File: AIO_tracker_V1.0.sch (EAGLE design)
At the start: 60 parts, among them IC1 TPS61201, IC2 TPS61201, J1 AVR_SPI_PRG_6PTH, Q1 MOSFET-PCHANNELSMD, U1 ATMEGA328P-AU, U2 USD-SOCKETNEW

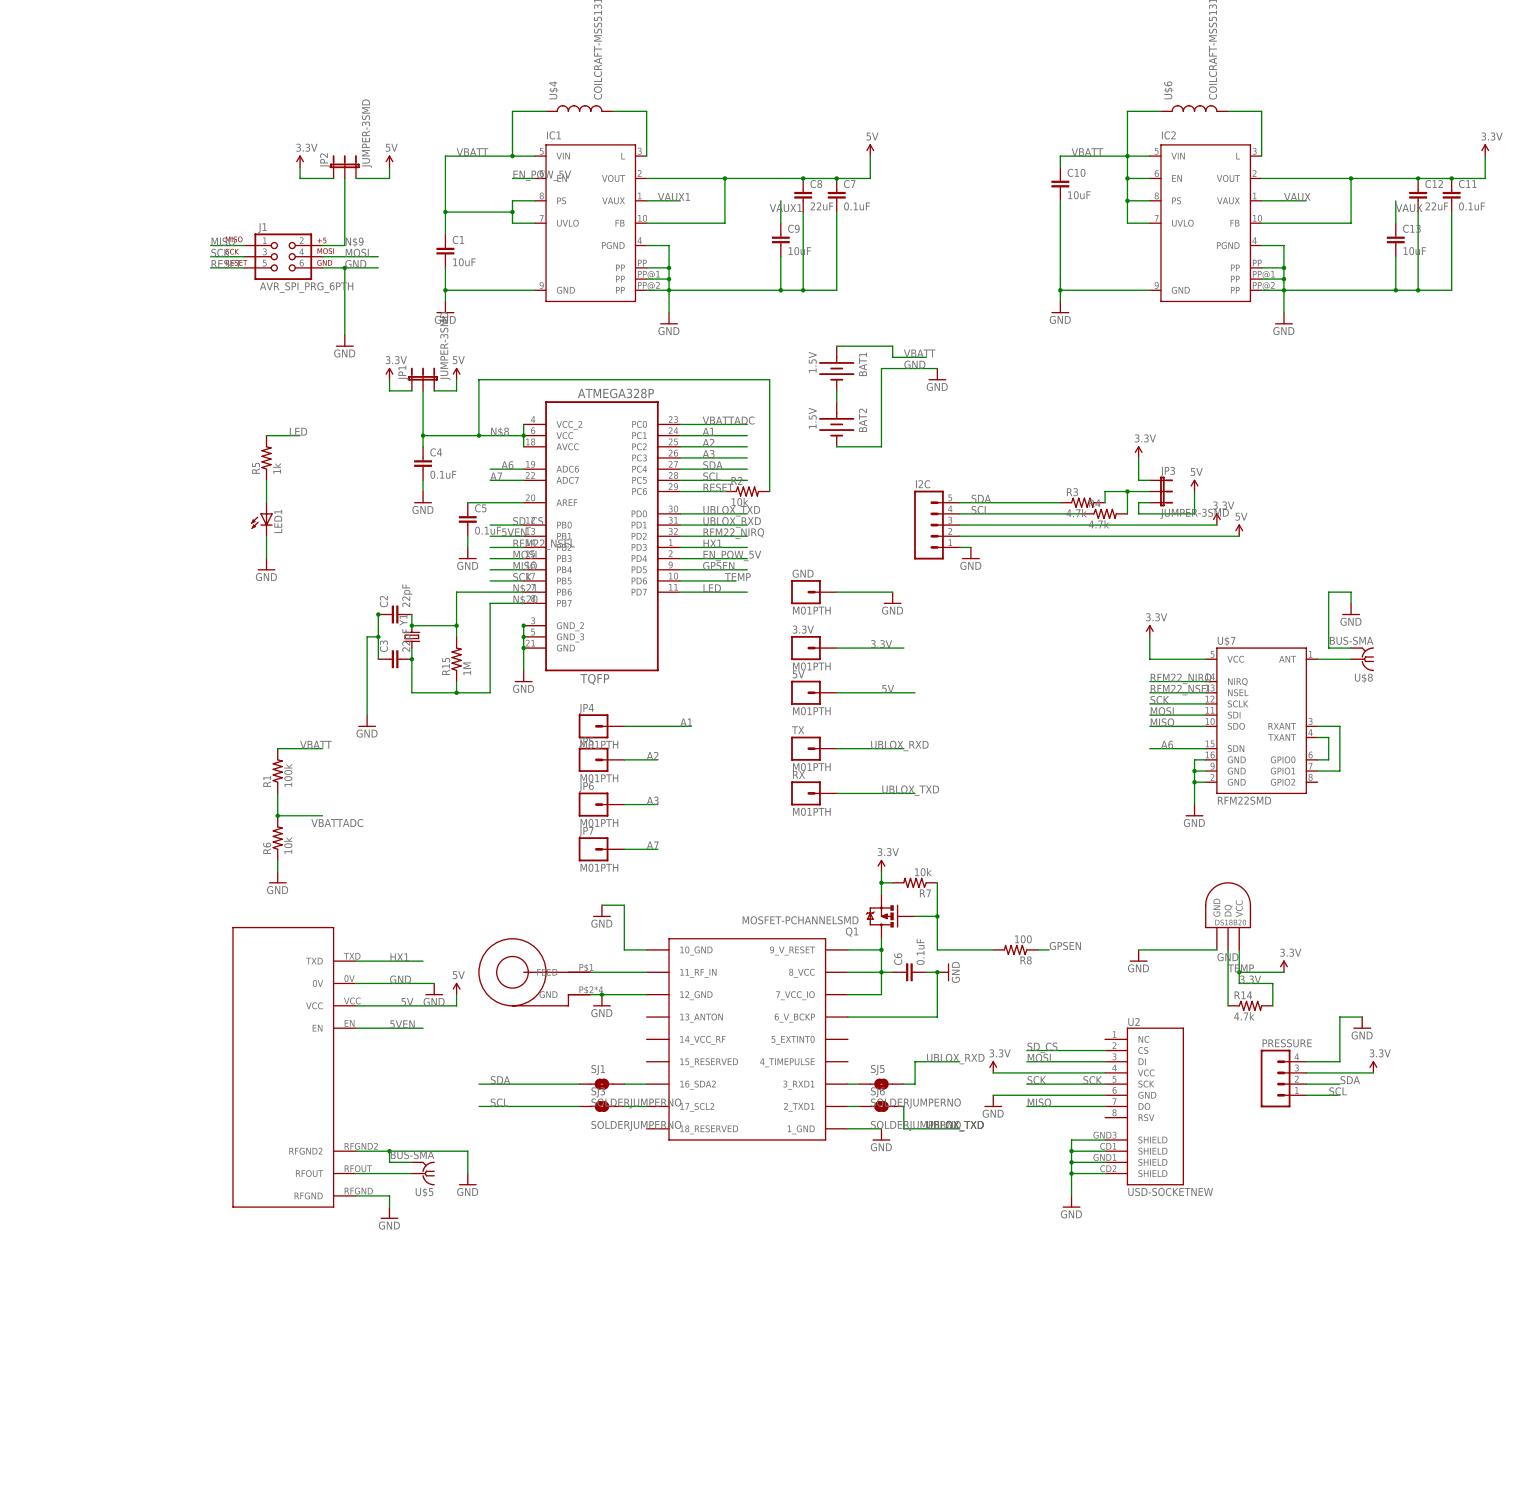
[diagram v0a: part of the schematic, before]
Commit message: Added NTX2 Support option
Added NTX2 Support option and finished routing
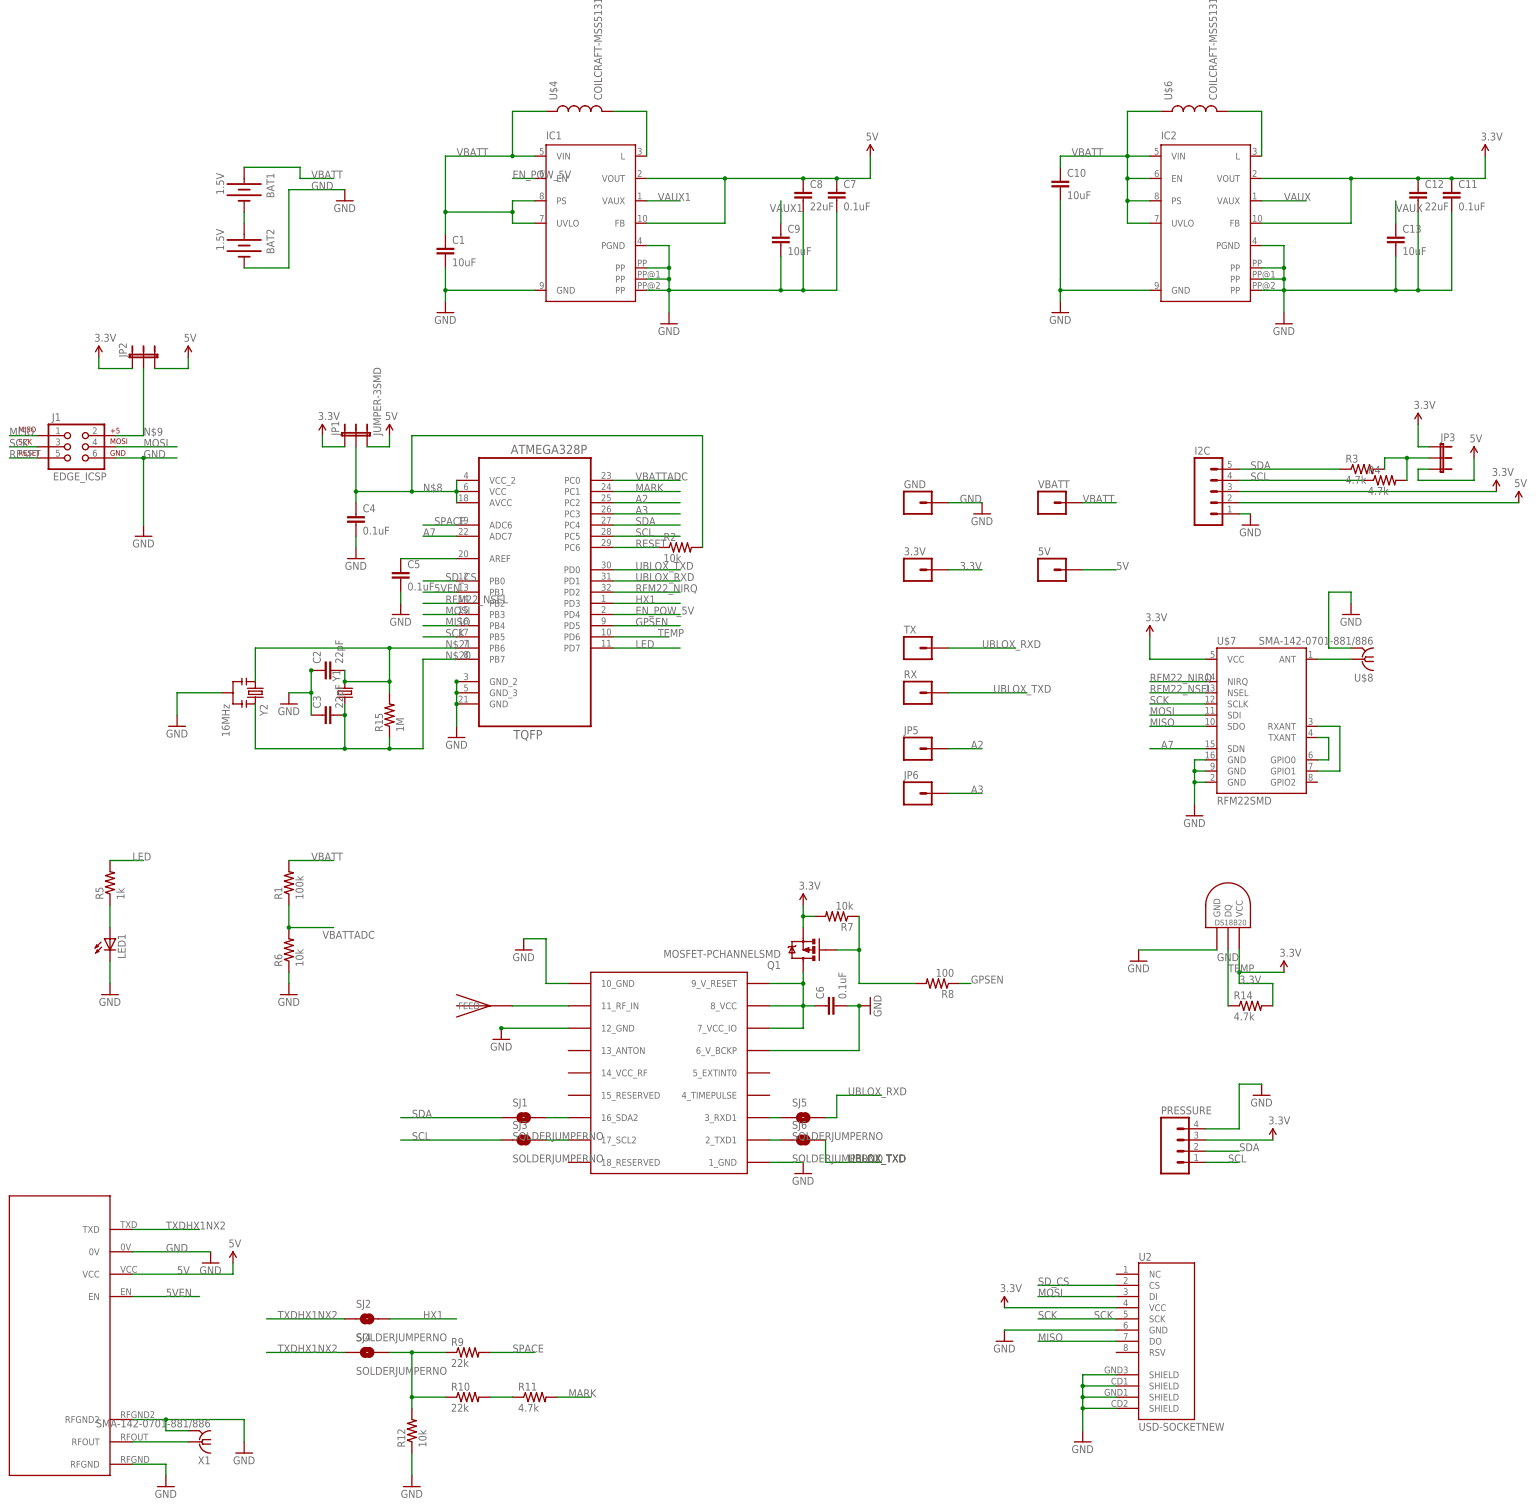
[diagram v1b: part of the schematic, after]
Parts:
- removed JP4, JP7: M01PTH, SparkFun-Connectors:M01PTH
- removed U$5: BUS-SMA, Ava:BUS-SMA
- added R10, R9: 22k, SparkFun-Passives:RESISTOR0603-RES
- added R11: 4.7k, SparkFun-Passives:RESISTOR0603-RES
- added R12: 10k, SparkFun-Passives:RESISTOR0603-RES
- added SJ2, SJ4: SOLDERJUMPERNO, SparkFun-Passives:SOLDERJUMPERNO
- added VBATT: M01SMDNS, SparkFun-Connectors:M01SMDNS
- added X1: SMA-142-0701-881/886, con-coax:SMA-142-0701-881/886
- added Y2: 16MHz, SparkFun-FreqCtrl:RESONATOR16MHZ
- 3.3V, 5V, GND: value M01PTH -> M01SMDNS; device SparkFun-Connectors:M01PTH -> SparkFun-Connectors:M01SMDNS
- J1: value AVR_SPI_PRG_6PTH -> EDGE_ICSP; device SparkFun-Connectors:AVR_SPI_PRG_6PTH -> Ava:EDGE_ICSP
- U$2: value JDGA-REMQV-ANTENNA -> JTI_ANTENNA-1575AT43A40; device Ava:JDGA-REMQV-ANTENNA -> Ava:JTI_ANTENNA-1575AT43A40
- U$8: value BUS-SMA -> SMA-142-0701-881/886; device Ava:BUS-SMA -> con-coax:SMA-142-0701-881/886
- U$9: value DS1820TO92 -> DS1820; device Ava:DS1820TO92 -> Ava:DS1820
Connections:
- removed net A1: JP4.1, U1.PC1
- removed net A6: U$7.SDN, U1.ADC6
- new net MARK: R11.2, U1.PC1
- new net N$17: R10.1, R12.2, R9.1, SJ4.2
- new net N$18: R10.2, R11.1
- new net SPACE: R9.2, U1.ADC6
- new net TXDHX1NX2: SJ2.1, SJ4.1, U$3.TXD
- net A7: now also U$7.SDN; no longer JP7.1
- net GND: now also R12.1, U$8.2, X1.2, Y2.2; no longer U$2.GND, U$5.GND, U$8.GND
- net HX1: now also SJ2.2; no longer U$3.TXD
- net N$20: now also Y2.3
- net N$21: now also Y2.1
- net N$5: now also X1.1; no longer U$5.1
- net VBATT: now also VBATT.1
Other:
- moved on the sheet: 3.3V, 5V, BAT1, BAT2, C2, C3, C4, C5, C6, GND, I2C, J1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

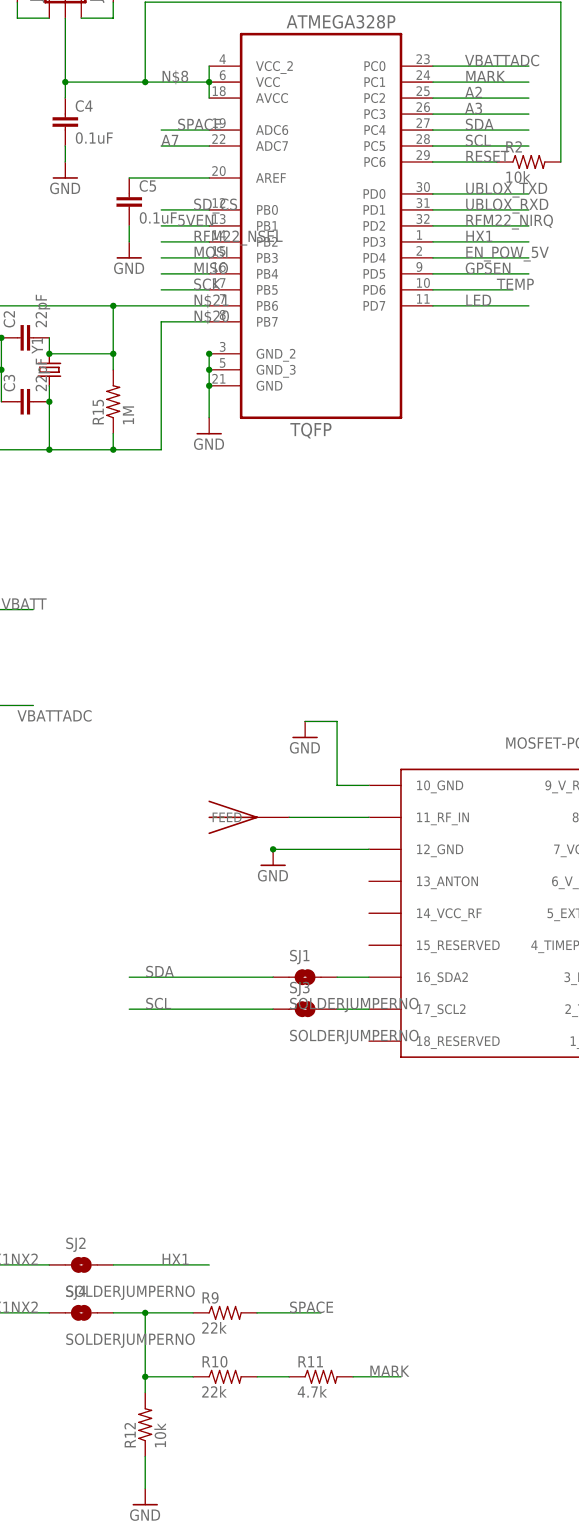
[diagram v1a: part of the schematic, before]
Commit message: corrected a few erros with the NTX2
Added back pads to the HX1 footprint, corrected the voltage divider,
corrected the antenna layout, changed SDN of RFM22b to the A7, corrected
the values in the schematic

Missing:
- Cuttof system
- New pressure sensor
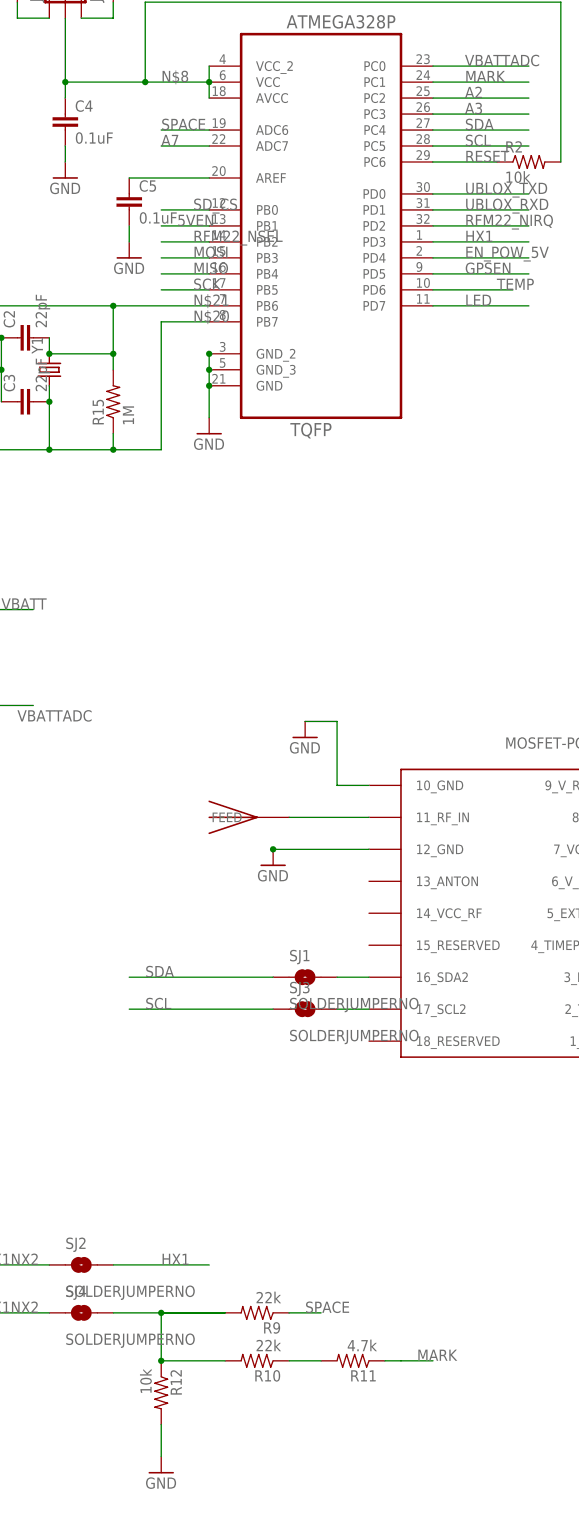
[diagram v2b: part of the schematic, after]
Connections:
- net GND: now also R12.2; no longer R12.1
- net MARK: now also R11.1; no longer R11.2
- net N$17: now also R10.2, R12.1, R9.2; no longer R10.1, R12.2, R9.1
- net N$18: now also R10.1, R11.2; no longer R10.2, R11.1
- net SPACE: now also R9.1; no longer R9.2
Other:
- moved on the sheet: R10, R11, R12, R9
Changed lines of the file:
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@@
 <instance part="SJ2" gate="1" x="-15.24" y="-193.04"/>
 <instance part="SJ4" gate="1" x="-15.24" y="-200.66"/>
-<instance part="R9" gate="G$1" x="7.62" y="-200.66"/>
-<instance part="R10" gate="G$1" x="7.62" y="-210.82"/>
-<instance part="R11" gate="G$1" x="22.86" y="-210.82"/>
-<instance part="R12" gate="G$1" x="-5.08" y="-218.44" rot="R90"/>
-<instance part="GND28" gate="1" x="-5.08" y="-231.14"/>
+<instance part="R9" gate="G$1" x="12.7" y="-200.66" rot="R180"/>
+<instance part="R10" gate="G$1" x="12.7" y="-208.28" rot="R180"/>
+<instance part="R11" gate="G$1" x="27.94" y="-208.28" rot="R180"/>
+<instance part="R12" gate="G$1" x="-2.54" y="-213.36" rot="R270"/>
+<instance part="GND28" gate="1" x="-2.54" y="-226.06"/>
 </instances>
 <busses>
@@
 </segment>
 <segment>
-<wire x1="-5.08" y1="-223.52" x2="-5.08" y2="-228.6" width="0.1524" layer="91"/>
-<pinref part="R12" gate="G$1" pin="1"/>
+<pinref part="R12" gate="G$1" pin="2"/>
+<wire x1="-2.54" y1="-223.52" x2="-2.54" y2="-218.44" width="0.1524" layer="91"/>
 <pinref part="GND28" gate="1" pin="GND"/>
 </segment>
@@
 </segment>
 </net>
-<net name="N$17" class="0">
-<segment>
-<pinref part="SJ4" gate="1" pin="2"/>
-<pinref part="R12" gate="G$1" pin="2"/>
-<wire x1="-10.16" y1="-200.66" x2="-5.08" y2="-200.66" width="0.1524" layer="91"/>
-<wire x1="-5.08" y1="-200.66" x2="-5.08" y2="-210.82" width="0.1524" layer="91"/>
-<pinref part="R9" gate="G$1" pin="1"/>
-<wire x1="-5.08" y1="-210.82" x2="-5.08" y2="-213.36" width="0.1524" layer="91"/>
-<wire x1="2.54" y1="-200.66" x2="-5.08" y2="-200.66" width="0.1524" layer="91"/>
-<pinref part="R10" gate="G$1" pin="1"/>
-<wire x1="2.54" y1="-210.82" x2="-5.08" y2="-210.82" width="0.1524" layer="91"/>
-<junction x="-5.08" y="-200.66"/>
-<junction x="-5.08" y="-210.82"/>
-</segment>
-</net>
-<net name="N$18" class="0">
-<segment>
-<pinref part="R10" gate="G$1" pin="2"/>
-<pinref part="R11" gate="G$1" pin="1"/>
-<wire x1="12.7" y1="-210.82" x2="17.78" y2="-210.82" width="0.1524" layer="91"/>
-</segment>
-</net>
 <net name="MARK" class="0">
 <segment>
@@
 </segment>
 <segment>
-<pinref part="R11" gate="G$1" pin="2"/>
-<wire x1="27.94" y1="-210.82" x2="35.56" y2="-210.82" width="0.1524" layer="91"/>
-<label x="30.48" y="-210.82" size="1.778" layer="95"/>
-</segment>
-</net>
-<net name="SPACE" class="0">
-<segment>
-<pinref part="U1" gate="A" pin="ADC6"/>
-<wire x1="5.08" y1="-12.7" x2="-2.54" y2="-12.7" width="0.1524" layer="91"/>
-<label x="0" y="-12.7" size="1.778" layer="95"/>
-</segment>
-<segment>
-<pinref part="R9" gate="G$1" pin="2"/>
-<wire x1="12.7" y1="-200.66" x2="22.86" y2="-200.66" width="0.1524" layer="91"/>
-<label x="17.78" y="-200.66" size="1.778" layer="95"/>
+<wire x1="35.56" y1="-208.28" x2="40.64" y2="-208.28" width="0.1524" layer="91"/>
+<pinref part="R11" gate="G$1" pin="1"/>
+<wire x1="35.56" y1="-208.28" x2="33.02" y2="-208.28" width="0.1524" layer="91"/>
+<label x="38.1" y="-208.28" size="1.778" layer="95"/>
 </segment>
 </net>
@@
 </segment>
 </net>
+<net name="SPACE" class="0">
+<segment>
+<pinref part="U1" gate="A" pin="ADC6"/>
+<wire x1="5.08" y1="-12.7" x2="-2.54" y2="-12.7" width="0.1524" layer="91"/>
+<label x="-2.54" y="-12.7" size="1.778" layer="95"/>
+</segment>
+<segment>
+<pinref part="R9" gate="G$1" pin="1"/>
+<wire x1="17.78" y1="-200.66" x2="22.86" y2="-200.66" width="0.1524" layer="91"/>
+<label x="20.32" y="-200.66" size="1.778" layer="95"/>
+</segment>
+</net>
+<net name="N$17" class="0">
+<segment>
+<pinref part="SJ4" gate="1" pin="2"/>
+<pinref part="R9" gate="G$1" pin="2"/>
+<wire x1="-10.16" y1="-200.66" x2="-2.54" y2="-200.66" width="0.1524" layer="91"/>
+<pinref part="R12" gate="G$1" pin="1"/>
+<wire x1="-2.54" y1="-200.66" x2="7.62" y2="-200.66" width="0.1524" layer="91"/>
+<wire x1="7.62" y1="-200.66" x2="-2.54" y2="-200.66" width="0.1524" layer="91"/>
+<wire x1="-2.54" y1="-200.66" x2="-2.54" y2="-208.28" width="0.1524" layer="91"/>
+<pinref part="R10" gate="G$1" pin="2"/>
+<wire x1="-2.54" y1="-208.28" x2="7.62" y2="-208.28" width="0.1524" layer="91"/>
+<junction x="-2.54" y="-208.28"/>
+<junction x="-2.54" y="-200.66"/>
+</segment>
+</net>
+<net name="N$18" class="0">
+<segment>
+<pinref part="R10" gate="G$1" pin="1"/>
+<pinref part="R11" gate="G$1" pin="2"/>
+<wire x1="17.78" y1="-208.28" x2="22.86" y2="-208.28" width="0.1524" layer="91"/>
+</segment>
+</net>
